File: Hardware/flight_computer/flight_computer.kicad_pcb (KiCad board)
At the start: 4 copper layers, 80 x 100 mm, 120 parts, among them J1 Micro_USB, J2 MicroSD_molex, J3 rpi_zero_w, J4 JST_8_RA, J5 JST_GH_6_RA, J6 JST_GH_4_RA, J7 JST_GH_5_RA, J8 Conn_02x03, J9 Conn_02x03, Q2 PMOS_20V_.76A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

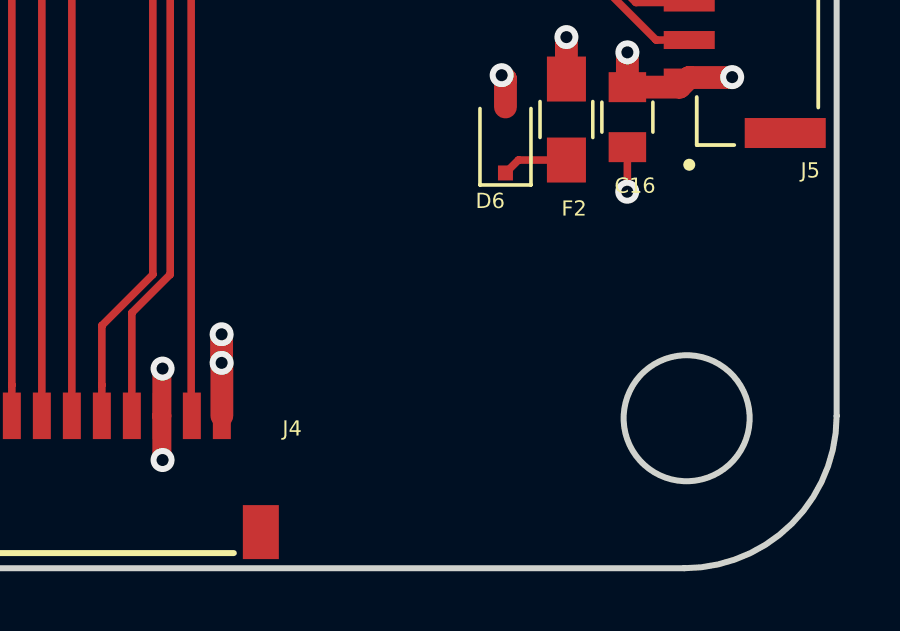
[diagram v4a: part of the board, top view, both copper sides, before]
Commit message: Adds 2-pin battery connector
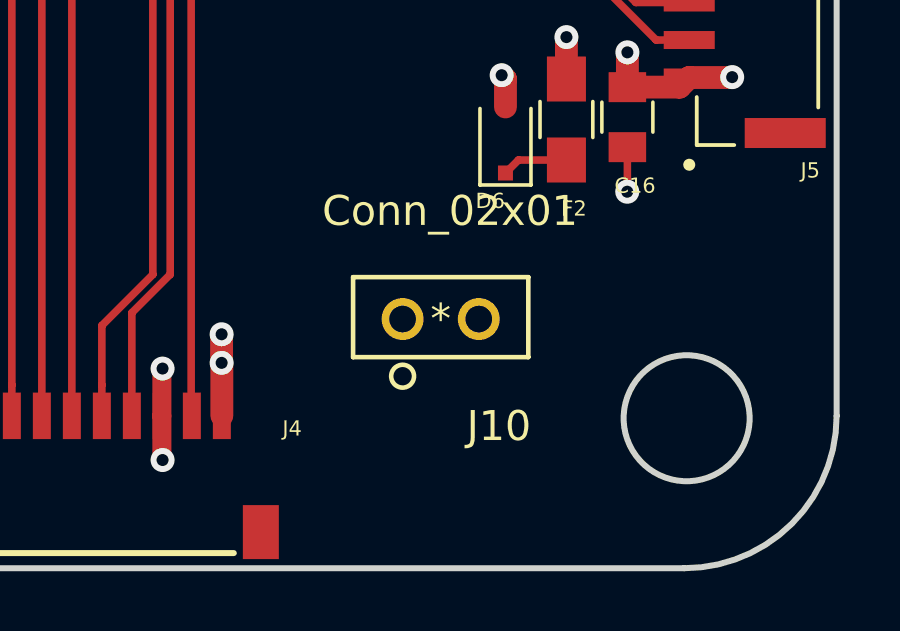
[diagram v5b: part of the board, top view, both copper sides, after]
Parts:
- added J10: Conn_02x01, drone_footprints:TSW-102-07-F-S, F.Cu at (146.3, 152.1)
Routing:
- net /VBAT: track 41.0 -> 48.9 mm
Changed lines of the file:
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@@
     (thickness 1.6)
     (drawings 29)
-    (tracks 1531)
+    (tracks 1534)
     (zones 0)
-    (modules 120)
+    (modules 121)
     (nets 184)
   )
@@
   )
   (setup
-    (last_trace_width 0.254)
+    (last_trace_width 0.762)
     (user_trace_width 0.381)
     (user_trace_width 0.508)
@@
       (net 183 "Net-(R37-Pad2)"))
   )
+  (module drone_footprints:TSW-102-07-F-S (layer F.Cu)
+    (at 146.304 152.146)
+    (fp_text reference J10 (at 1.94 3.57) (layer F.SilkS)
+      (effects (font (size 1 1) (thickness 0.15)))
+    )
+    (fp_text value Conn_02x01 (at 0.31 -3.6) (layer F.SilkS)
+      (effects (font (size 1 1) (thickness 0.15)))
+    )
+    (fp_line (start -2.921 1.27) (end 2.921 1.27) (layer F.SilkS) (width 0.1524))
+    (fp_line (start 2.921 1.27) (end 2.921 -1.397) (layer F.SilkS) (width 0.1524))
+    (fp_line (start 2.921 -1.397) (end -2.921 -1.397) (layer F.SilkS) (width 0.1524))
+    (fp_line (start -2.921 -1.397) (end -2.921 1.27) (layer F.SilkS) (width 0.1524))
+    (fp_line (start -2.794 1.143) (end 2.794 1.143) (layer F.Fab) (width 0.1524))
+    (fp_line (start 2.794 1.143) (end 2.794 -1.27) (layer F.Fab) (width 0.1524))
+    (fp_line (start 2.794 -1.27) (end -2.794 -1.27) (layer F.Fab) (width 0.1524))
+    (fp_line (start -2.794 -1.27) (end -2.794 1.143) (layer F.Fab) (width 0.1524))
+    (fp_line (start 2.54 -1.524) (end 2.54 -2.5908) (layer F.CrtYd) (width 0.1524))
+    (fp_line (start 2.54 -2.5908) (end -2.54 -2.5908) (layer F.CrtYd) (width 0.1524))
+    (fp_line (start -2.54 -2.5908) (end -2.54 -1.524) (layer F.CrtYd) (width 0.1524))
+    (fp_line (start -2.54 -1.524) (end -3.048 -1.524) (layer F.CrtYd) (width 0.1524))
+    (fp_line (start -3.048 -1.524) (end -3.048 1.397) (layer F.CrtYd) (width 0.1524))
+    (fp_line (start -3.048 1.397) (end -2.54 1.397) (layer F.CrtYd) (width 0.1524))
+    (fp_line (start -2.54 1.397) (end -2.54 2.5908) (layer F.CrtYd) (width 0.1524))
+    (fp_line (start -2.54 2.5908) (end 2.54 2.5908) (layer F.CrtYd) (width 0.1524))
+    (fp_line (start 2.54 2.5908) (end 2.54 1.397) (layer F.CrtYd) (width 0.1524))
+    (fp_line (start 2.54 1.397) (end 3.048 1.397) (layer F.CrtYd) (width 0.1524))
+    (fp_line (start 3.048 1.397) (end 3.048 -1.524) (layer F.CrtYd) (width 0.1524))
+    (fp_line (start 3.048 -1.524) (end 2.54 -1.524) (layer F.CrtYd) (width 0.1524))
+    (fp_circle (center -1.27 1.905) (end -0.889 1.905) (layer F.SilkS) (width 0.1524))
+    (fp_circle (center -1.27 1.905) (end -0.889 1.905) (layer B.SilkS) (width 0.1524))
+    (fp_circle (center -1.27 0) (end -1.016 0) (layer F.Fab) (width 0.1524))
+    (fp_text user "Copyright 2016 Accelerated Designs. All rights reserved." (at 0 0) (layer Cmts.User)
+      (effects (font (size 0.127 0.127) (thickness 0.002)))
+    )
+    (fp_text user * (at 0 0) (layer F.SilkS)
+      (effects (font (size 1 1) (thickness 0.15)))
+    )
+    (fp_text user * (at 0 0) (layer F.Fab)
+      (effects (font (size 1 1) (thickness 0.15)))
+    )
+    (pad 1 thru_hole circle (at -1.27 0 90) (size 1.397 1.397) (drill 0.889) (layers *.Cu *.Mask)
+      (net 10 /VBAT))
+    (pad 2 thru_hole circle (at 1.27 0 90) (size 1.397 1.397) (drill 0.889) (layers *.Cu *.Mask)
+      (net 1 GND))
+  )
   (gr_text 5V (at 109.982 83.566) (layer F.SilkS)
     (effects (font (size 0.762 0.762) (thickness 0.127)))
@@
   (segment (start 139.0015 152.654) (end 139.0015 148.717) (width 0.762) (layer In2.Cu) (net 10))
   (via (at 120.269 145.2245) (size 0.8) (drill 0.4) (layers F.Cu B.Cu) (net 10))
-  (segment (start 139.0015 148.717) (end 135.509 145.2245) (width 0.762) (layer In2.Cu) (net 10))
   (segment (start 135.509 145.2245) (end 120.269 145.2245) (width 0.762) (layer In2.Cu) (net 10))
   (segment (start 127.742901 147.902499) (end 127.742901 145.776901) (width 0.381) (layer F.Cu) (net 10))
@@
   (segment (start 127.1905 145.2245) (end 120.269 145.2245) (width 0.381) (layer F.Cu) (net 10))
   (segment (start 127.742901 145.776901) (end 127.1905 145.2245) (width 0.381) (layer F.Cu) (net 10))
+  (segment (start 142.4305 152.146) (end 138.65225 148.36775) (width 0.762) (layer In2.Cu) (net 10))
+  (segment (start 145.034 152.146) (end 142.4305 152.146) (width 0.762) (layer In2.Cu) (net 10))
+  (segment (start 139.0015 148.717) (end 138.65225 148.36775) (width 0.762) (layer In2.Cu) (net 10))
+  (segment (start 138.65225 148.36775) (end 135.509 145.2245) (width 0.762) (layer In2.Cu) (net 10))
   (segment (start 101.219 149.167) (end 101.277 149.167) (width 0.762) (layer F.Cu) (net 11))
   (segment (start 127.4605 152.8445) (end 127.508 152.892) (width 0.762) (layer F.Cu) (net 12))

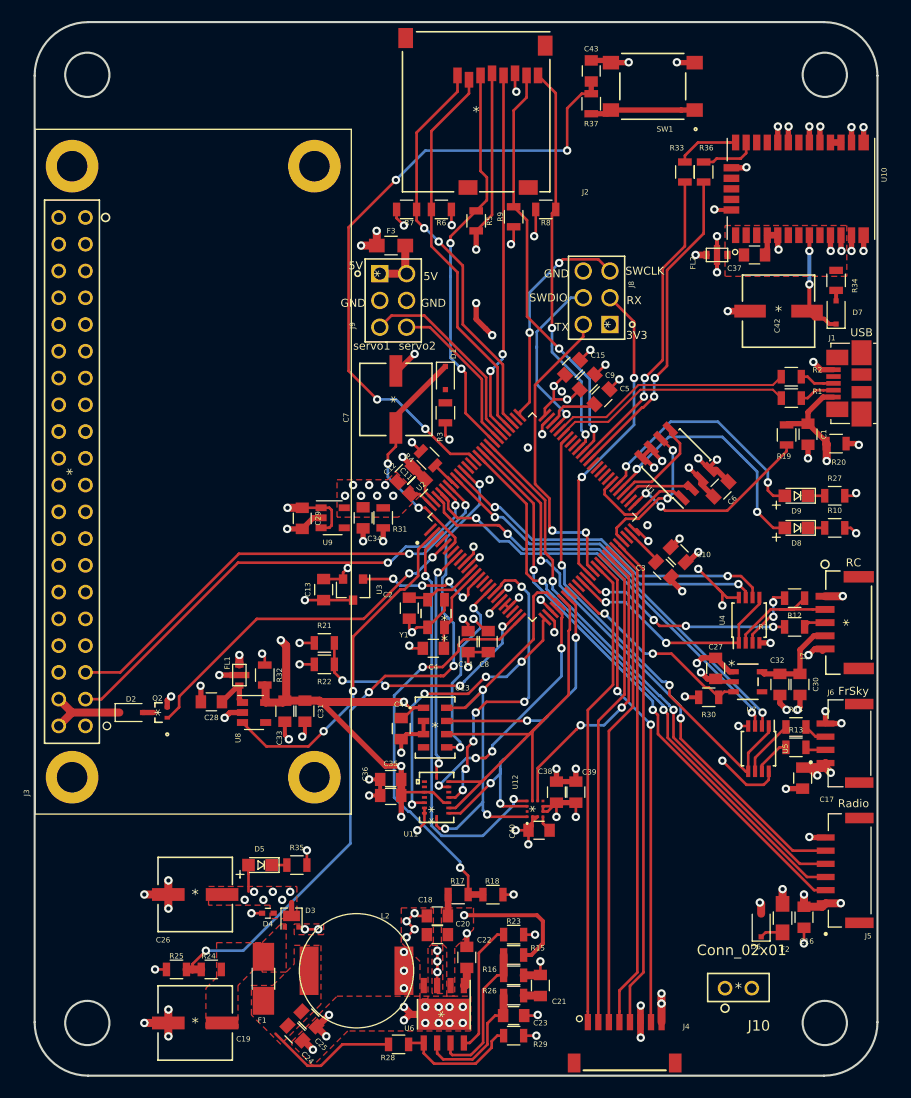
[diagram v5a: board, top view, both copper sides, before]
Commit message: fixed BMI088 footprint. Worked on layout
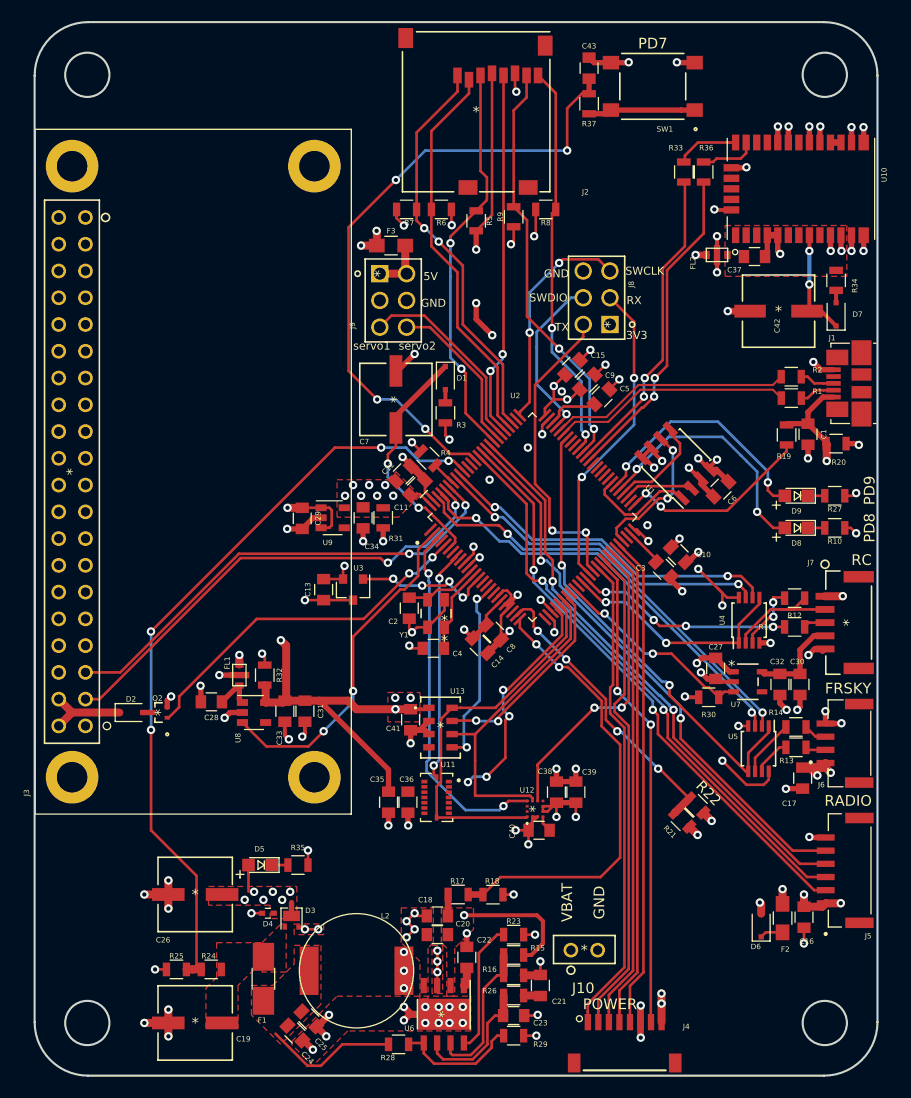
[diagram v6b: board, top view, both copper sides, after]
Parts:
- moved R21 37.9 mm to (141.0, 136.1), turned to 135 degrees
- moved R22 37.8 mm to (142.3, 134.8), turned to 315 degrees
- moved J10 15.1 mm to (131.7, 148.5)
- moved C35 2.17 mm to (113.1, 134.5), turned to 90 degrees
- moved C36 1.75 mm to (114.9, 134.5), turned to 270 degrees
- moved C41 1.22 mm to (115.2, 126.7)
- moved C14 1.20 mm to (121.8, 119.6), turned to 315 degrees
- moved C8 1.02 mm to (123.1, 118.4), turned to 315 degrees
- moved U13 0.51 mm to (118.0, 127.4)
- moved C43 0.34 mm to (132.1, 64.8)
- moved R37 0.20 mm to (132.1, 68.2)
- moved C12 0.18 mm to (114.5, 103.3)
- moved D7 0.18 mm to (155.6, 88.2)
- moved C37 0.15 mm to (147.8, 82.7)
- moved C11 0.10 mm to (115.8, 104.6)
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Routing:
- net /GYRO_DRDY: track 29.4 -> 0.00 mm, vias 6 -> 0
- net /IMU_GYRO_CS: track 27.9 -> 0.00 mm, vias 4 -> 0
- net /SENSOR_MOSI: track 43.3 -> 19.6 mm, vias 4 -> 2
- net /SENSOR_MISO: track 45.5 -> 30.6 mm
- net /VDD_3V3_SENSORS: track 119.6 -> 108.8 mm
- net /VDD_BUCK_VALID: track 67.3 -> 73.3 mm
- net /SENSOR_SCK: track 42.4 -> 36.7 mm, vias 3 -> 0
- net /MAG_CS: track 39.7 -> 34.5 mm
- net /VDD_3V3_STM: track 155.0 -> 160.0 mm, vias 36 -> 34
- net /VBAT_SENSE: track 38.6 -> 42.9 mm
- net /VDD_5V_SENSE: track 24.4 -> 28.0 mm
- net /VBAT: track 48.9 -> 46.3 mm
- net /IMU_ACCEL_CS: track 24.0 -> 21.9 mm
- net GND: track 244.4 -> 242.6 mm, vias 105 -> 103
- net Net-(D1-Pad2): track 0.00 -> 1.25 mm
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- added copper zone on F.Cu, net /VDD_3V3_SENSORS
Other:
- board text added: "FRSKY"
- board text added: "PD7"
- board text added: "PD8"
- board text added: "PD9"
- board text added: "POWER"
- board text added: "RADIO"
- board text added: "VBAT"
- board text removed: "FrSky"
- board text removed: "Radio"
- board text removed: "USB"

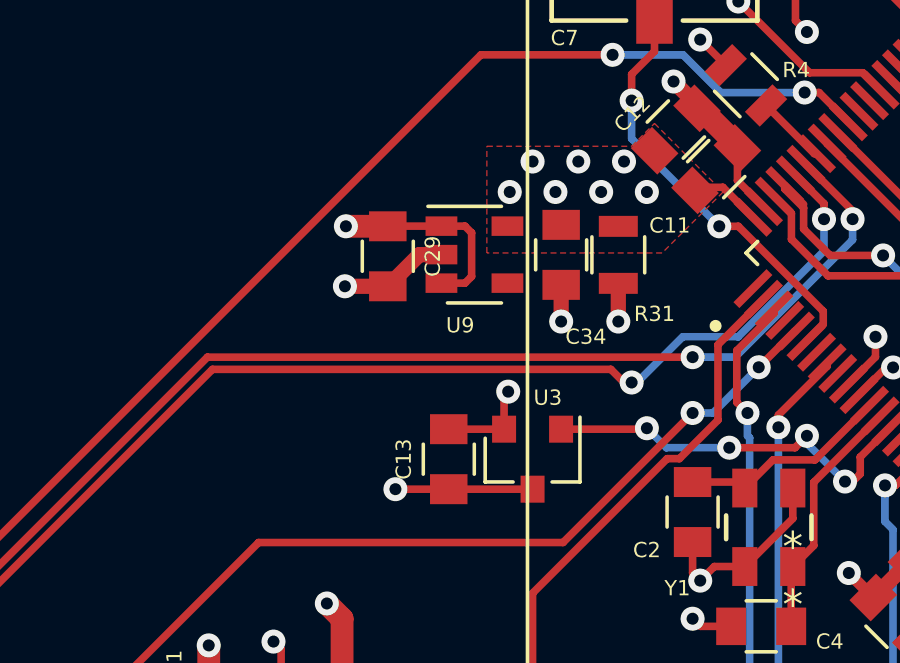
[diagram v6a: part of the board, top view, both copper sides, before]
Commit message: Adds i2c pullup resistors
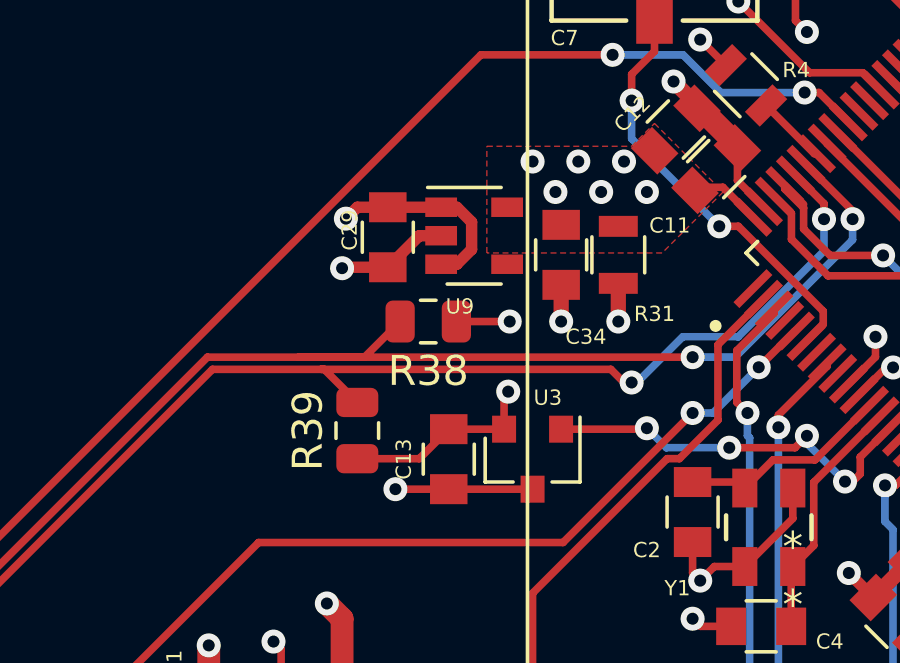
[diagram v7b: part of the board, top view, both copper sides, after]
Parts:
- added R38: R_10K, drone_footprints:R_0805, F.Cu at (106.3, 109.7)
- added R39: R_10K, drone_footprints:R_0805, F.Cu at (103.9, 113.4)
- moved C29 0.63 mm to (104.9, 106.9)
- moved U9 0.63 mm to (107.8, 106.9)
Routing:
- net /VDD_3V3_STM: track 160.0 -> 165.2 mm
- net /RASPI_I2C1_SCL: track 45.5 -> 49.4 mm
- net /RASPI_I2C1_SDA: track 45.8 -> 47.5 mm

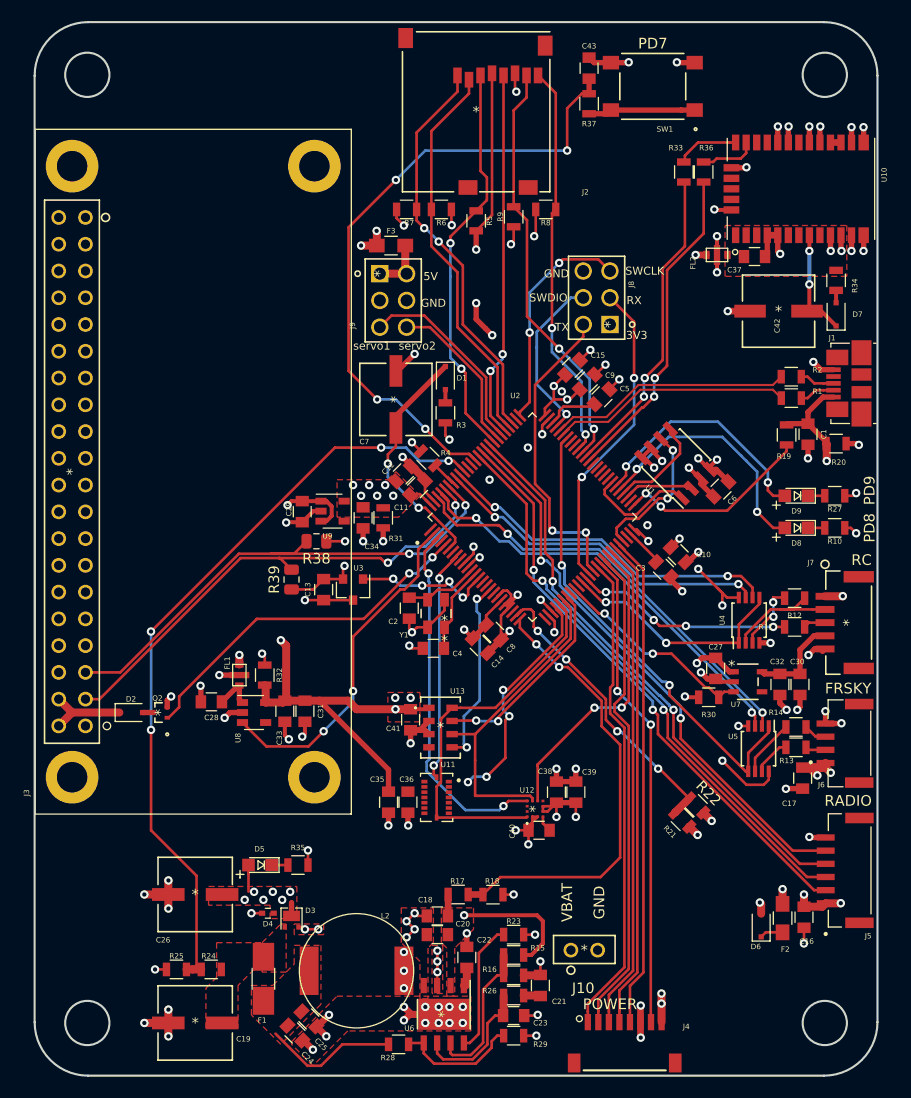
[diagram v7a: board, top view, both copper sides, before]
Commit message: finished sensor tracing. Added graphics and touched up front silk
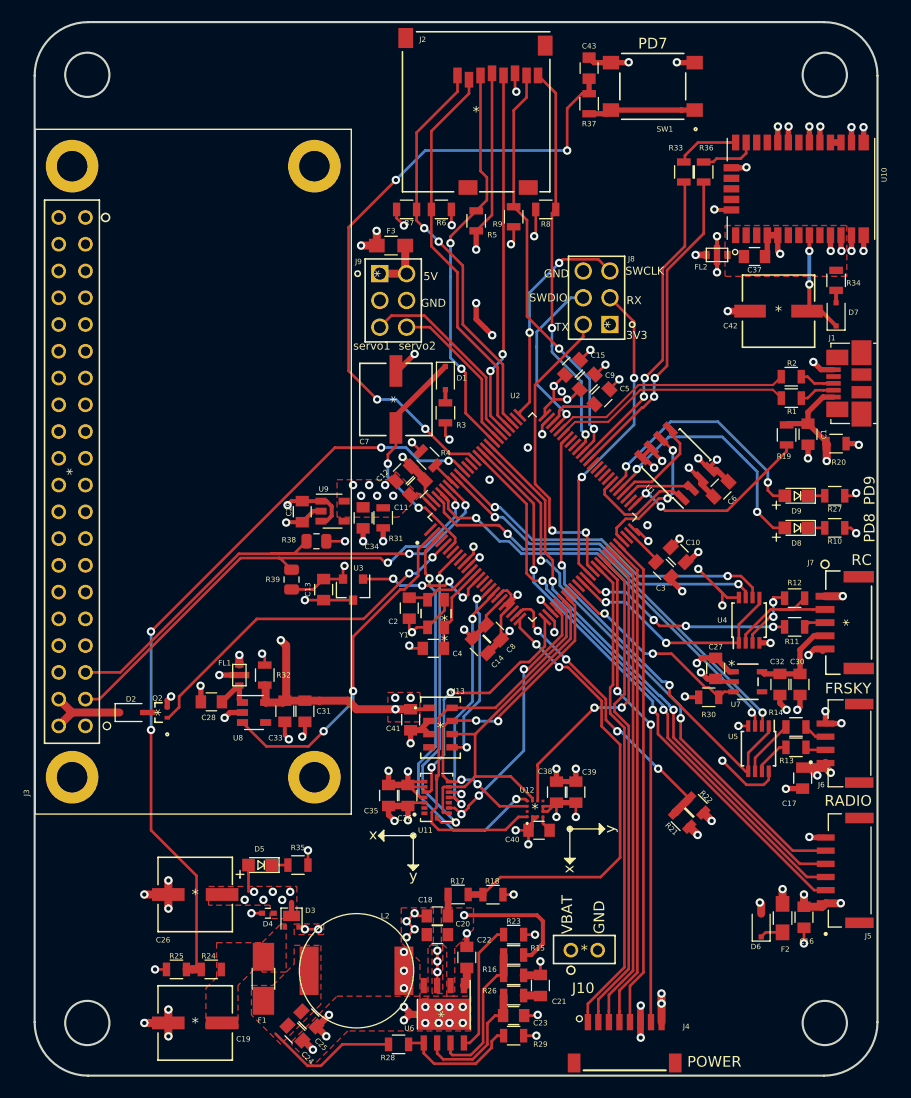
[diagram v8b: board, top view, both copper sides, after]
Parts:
- added G***: LOGO, drone_footprints:osprey_bitmap, B.Cu at (126.0, 123.6)
- moved C35 0.63 mm to (113.1, 133.9), turned to 270 degrees
- moved C36 0.63 mm to (114.9, 133.9), turned to 90 degrees
- turned U11 to 90 degrees
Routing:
- net /IMU_GYRO_CS: track 0.00 -> 24.2 mm, vias 0 -> 2
- net /GYRO_DRDY: track 0.00 -> 23.4 mm, vias 0 -> 2
- net /SENSOR_MOSI: track 19.6 -> 34.6 mm, vias 2 -> 4
- net /ACCEL_DRDY: track 22.0 -> 30.0 mm
- net GND: track 242.7 -> 250.2 mm
- net /SENSOR_MISO: track 30.6 -> 35.9 mm
- net /MAG_CS: track 34.5 -> 39.1 mm
- net /VDD_3V3_SENSORS: track 108.8 -> 105.3 mm, vias 7 -> 10
- net /IMU_ACCEL_CS: track 21.9 -> 25.5 mm, vias 4 -> 3
- net /SENSOR_SCK: track 36.7 -> 38.7 mm
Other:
- board text added: "x"
- board text added: "y"
